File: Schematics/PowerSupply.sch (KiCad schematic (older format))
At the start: 10 parts, among them Q1 2N7000, U1 LM2575-5.0BT, U2 LM3940

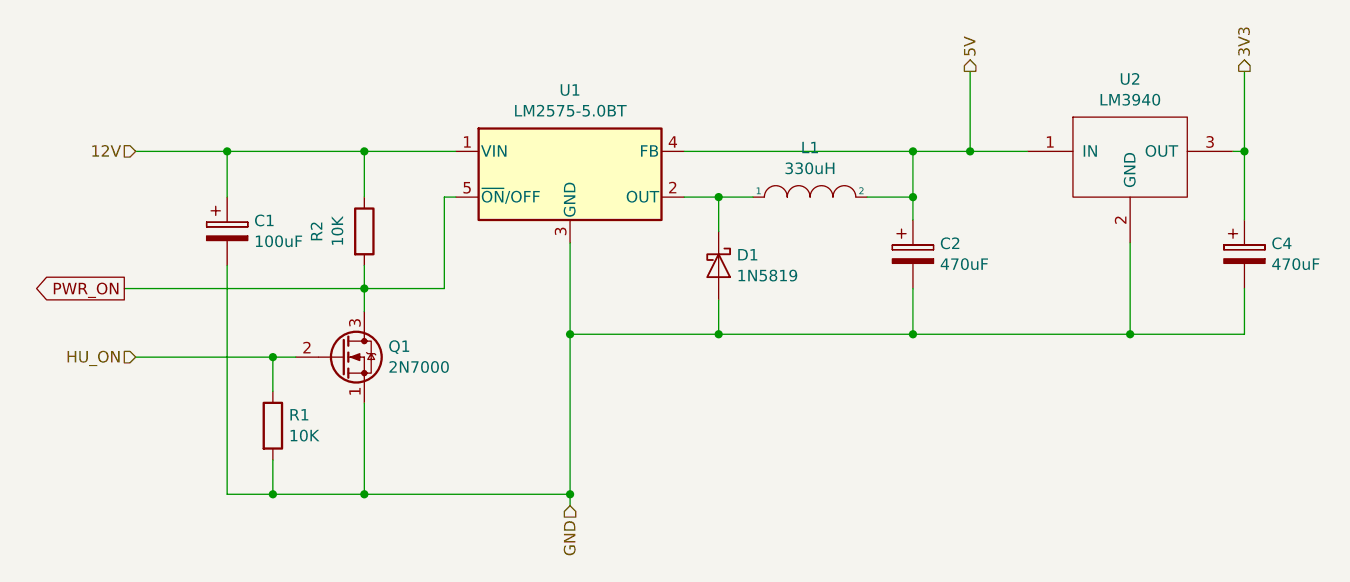
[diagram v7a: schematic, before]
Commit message: Updated power supply schematic and PCB design
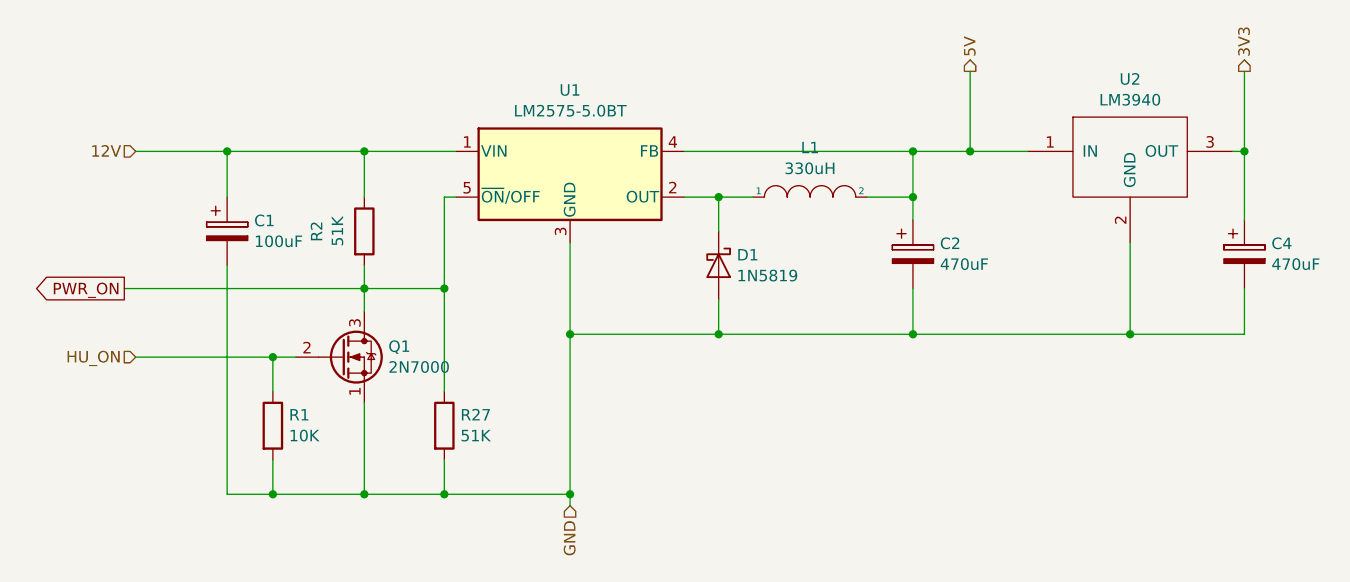
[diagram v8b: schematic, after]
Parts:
- added R27: 51K, Resistor_THT:R_Axial_DIN0207_L6.3mm_D2.5mm_P10.16mm_Horizontal, symbol Device:R
- R2: value 10K -> 51K
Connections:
- net GND: now also R27.2
- net PWR_ON: now also R27.1
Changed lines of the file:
@@
 EESchema Schematic File Version 4
 LIBS:RenaultBT-cache
-EELAYER 29 0
+EELAYER 26 0
 EELAYER END
 $Descr A4 11693 8268
@@
 AR Path="/5CC08323/5CC092F6" Ref="R2"  Part="1"
 F 0 "R2" V 4243 3450 50  0000 C CNN
-F 1 "10K" V 4334 3450 50  0000 C CNN
+F 1 "51K" V 4334 3450 50  0000 C CNN
 F 2 "Resistor_THT:R_Axial_DIN0207_L6.3mm_D2.5mm_P10.16mm_Horizontal" V 4380 3450 50  0001 C CNN
 F 3 "~" H 4450 3450 50  0001 C CNN
@@
 Connection ~ 4050 4600
 Wire Wire Line
-	4450 4600 5350 4600
+	4450 4600 4800 4600
 Wire Wire Line
 	5350 4600 5350 3900
@@
 	1    0    0    -1
 $EndComp
+$Comp
+L Device:R R27
+U 1 1 5D41D046
+P 4800 4300
+F 0 "R27" H 4870 4346 50  0000 L CNN
+F 1 "51K" H 4870 4255 50  0000 L CNN
+F 2 "Resistor_THT:R_Axial_DIN0207_L6.3mm_D2.5mm_P10.16mm_Horizontal" V 4730 4300 50  0001 C CNN
+F 3 "~" H 4800 4300 50  0001 C CNN
+	1    4800 4300
+	1    0    0    -1
+$EndComp
+Wire Wire Line
+	4800 4150 4800 3700
+Connection ~ 4800 3700
+Wire Wire Line
+	4800 4450 4800 4600
+Connection ~ 4800 4600
+Wire Wire Line
+	4800 4600 5350 4600
 $EndSCHEMATC
